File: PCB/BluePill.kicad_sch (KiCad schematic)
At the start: 36 parts, among them J1 USB_B_Micro, J2 Conn_01x20, J3 Conn_02x03_Odd_Even, J4 Conn_01x20, J5 Conn_01x04, SW1 SW_Push, U1 STM32F103C8Tx, U2 RT9193-33, Y1 Crystal_GND24_Small, Y2 8MHZ

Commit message: 更换USB插座封装
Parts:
- J1: value USB_B_Micro -> (none); footprint Connector_USB:USB_Micro-B_Molex_47346-0001 -> (none)
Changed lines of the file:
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@@
     (in_bom yes) (on_board yes) (fields_autoplaced)
     (property "Reference" "J1" (id 0) (at 43.18 19.05 0))
-    (property "Value" "USB_B_Micro" (id 1) (at 43.18 21.59 0))
-    (property "Footprint" "Connector_USB:USB_Micro-B_Molex_47346-0001" (id 2) (at 46.99 33.02 0)
+    (property "Value" "" (id 1) (at 43.18 21.59 0))
+    (property "Footprint" "" (id 2) (at 46.99 33.02 0)
       (effects (font (size 1.27 1.27)) hide)
     )
@@
     )
     (path "/5e707534-c918-46f7-a5cb-689e5a18b5bb"
-      (reference "J1") (unit 1) (value "USB_B_Micro") (footprint "Connector_USB:USB_Micro-B_Molex_47346-0001")
+      (reference "J1") (unit 1) (value "USB_B_Micro") (footprint "Connector_USB:USB_Micro-B_Molex-105017-0001")
     )
     (path "/7870a9db-0a4b-4ce4-a426-dcf645359822"

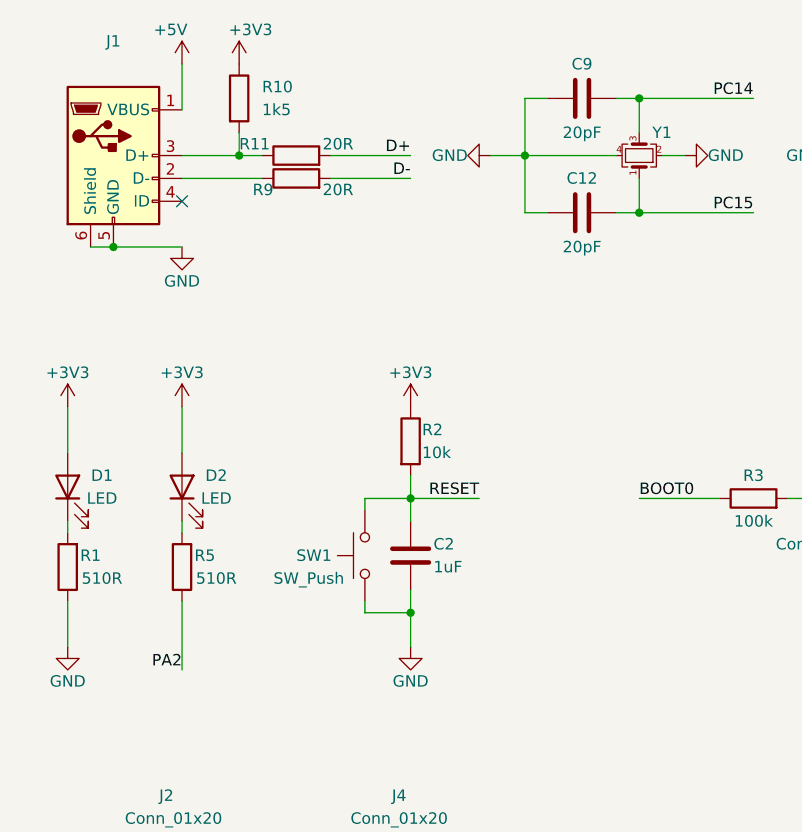
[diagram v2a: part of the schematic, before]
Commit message: 修复32K晶振问题；局部优化。
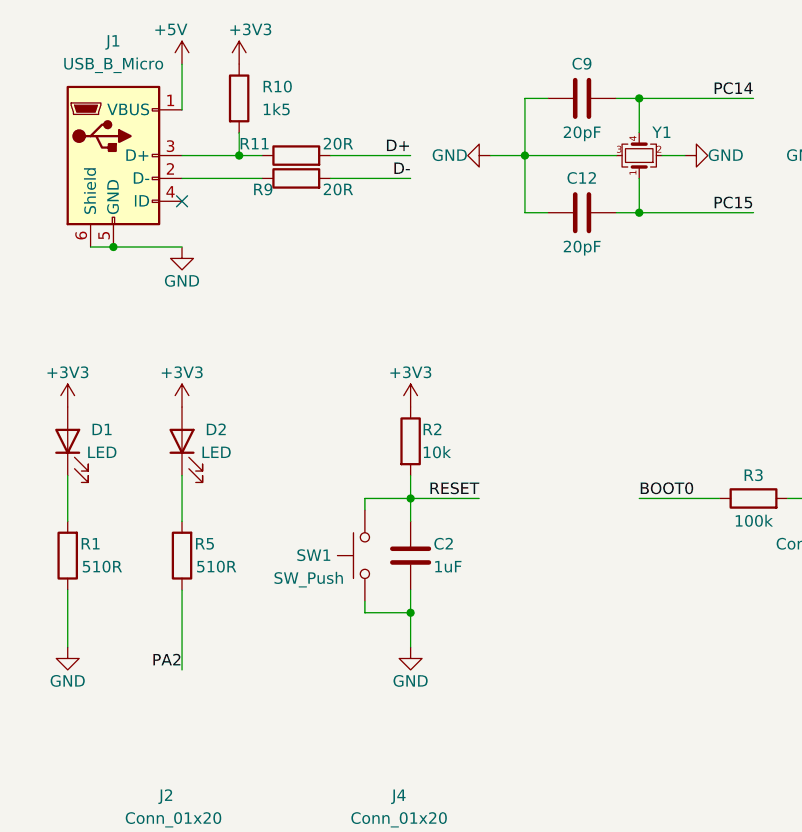
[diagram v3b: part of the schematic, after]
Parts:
- J1: value (none) -> USB_B_Micro; footprint (none) -> Connector_USB:USB_Micro-B_Molex-105017-0001
- Y1: value Crystal_GND24_Small -> (none); footprint Crystal:Crystal_SMD_SeikoEpson_MC306-4Pin_8.0x3.2mm -> (none); symbol Device:Crystal_GND24_Small -> Device:Crystal_GND23_Small
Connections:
- net GND: now also Y1.3; no longer Y1.4
- net PC14: now also Y1.4; no longer Y1.3
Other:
- moved on the sheet: D1, D2, R1, R5
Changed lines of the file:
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@@
+    (stroke (width 0) (type default) (color 0 0 0 0))
+  )
+  (wire (pts (xy 50.8 67.31) (xy 50.8 72.39))
     (stroke (width 0) (type default) (color 0 0 0 0))
   )
@@
     (stroke (width 0) (type default) (color 0 0 0 0))
   )
-  (wire (pts (xy 38.1 73.66) (xy 38.1 72.39))
-    (stroke (width 0) (type default) (color 0 0 0 0))
-  )
   (wire (pts (xy 106.68 31.75) (xy 104.14 31.75))
     (stroke (width 0) (type default) (color 0 0 0 0))
@@
     (stroke (width 0) (type default) (color 0 0 0 0))
   )
-  (wire (pts (xy 50.8 81.28) (xy 50.8 88.9))
+  (wire (pts (xy 50.8 80.01) (xy 50.8 88.9))
     (stroke (width 0) (type default) (color 0 0 0 0))
   )
@@
     (stroke (width 0) (type default) (color 0 0 0 0))
   )
-  (wire (pts (xy 38.1 59.69) (xy 38.1 64.77))
-    (stroke (width 0) (type default) (color 0 0 0 0))
-  )
   (wire (pts (xy 38.1 139.7) (xy 44.45 139.7))
     (stroke (width 0) (type default) (color 0 0 0 0))
@@
     (stroke (width 0) (type default) (color 0 0 0 0))
   )
-  (wire (pts (xy 50.8 59.69) (xy 50.8 64.77))
-    (stroke (width 0) (type default) (color 0 0 0 0))
-  )
   (wire (pts (xy 101.6 176.53) (xy 110.49 176.53))
     (stroke (width 0) (type default) (color 0 0 0 0))
@@
     (stroke (width 0) (type default) (color 0 0 0 0))
   )
+  (wire (pts (xy 38.1 67.31) (xy 38.1 72.39))
+    (stroke (width 0) (type default) (color 0 0 0 0))
+  )
   (wire (pts (xy 130.81 104.14) (xy 130.81 105.41))
     (stroke (width 0) (type default) (color 0 0 0 0))
@@
     (stroke (width 0) (type default) (color 0 0 0 0))
   )
-  (wire (pts (xy 38.1 81.28) (xy 38.1 86.36))
+  (wire (pts (xy 38.1 80.01) (xy 38.1 86.36))
     (stroke (width 0) (type default) (color 0 0 0 0))
   )
@@
     (stroke (width 0) (type default) (color 0 0 0 0))
   )
-  (wire (pts (xy 50.8 72.39) (xy 50.8 73.66))
-    (stroke (width 0) (type default) (color 0 0 0 0))
-  )
   (wire (pts (xy 215.9 73.66) (xy 215.9 80.01))
     (stroke (width 0) (type default) (color 0 0 0 0))
@@
     (effects (font (size 1.27 1.27)) (justify right bottom))
   )
-  (symbol (lib_id "Device:R") (at 38.1 77.47 180) (unit 1)
-    (in_bom yes) (on_board yes)
-    (property "Reference" "R1" (id 0) (at 40.64 76.2 0))
-    (property "Value" "510R" (id 1) (at 41.91 78.74 0))
-    (property "Footprint" "Capacitor_SMD:C_0603_1608Metric" (id 2) (at 39.878 77.47 90)
-      (effects (font (size 1.27 1.27)) hide)
-    )
-    (property "Datasheet" "~" (id 3) (at 38.1 77.47 0)
+  (symbol (lib_id "Device:R") (at 38.1 76.2 180) (unit 1)
+    (in_bom yes) (on_board yes)
+    (property "Reference" "R1" (id 0) (at 40.64 74.93 0))
+    (property "Value" "510R" (id 1) (at 41.91 77.47 0))
+    (property "Footprint" "Capacitor_SMD:C_0603_1608Metric" (id 2) (at 39.878 76.2 90)
+      (effects (font (size 1.27 1.27)) hide)
+    )
+    (property "Datasheet" "~" (id 3) (at 38.1 76.2 0)
       (effects (font (size 1.27 1.27)) hide)
     )
@@
     (in_bom yes) (on_board yes) (fields_autoplaced)
     (property "Reference" "J1" (id 0) (at 43.18 19.05 0))
-    (property "Value" "" (id 1) (at 43.18 21.59 0))
-    (property "Footprint" "" (id 2) (at 46.99 33.02 0)
+    (property "Value" "USB_B_Micro" (id 1) (at 43.18 21.59 0))
+    (property "Footprint" "Connector_USB:USB_Micro-B_Molex-105017-0001" (id 2) (at 46.99 33.02 0)
       (effects (font (size 1.27 1.27)) hide)
     )
@@
     (pin "6")
   )
-  (symbol (lib_id "Device:LED") (at 50.8 68.58 90) (unit 1)
-    (in_bom yes) (on_board yes)
-    (property "Reference" "D2" (id 0) (at 54.61 67.31 90))
-    (property "Value" "LED" (id 1) (at 54.61 69.85 90))
-    (property "Footprint" "Capacitor_SMD:C_0603_1608Metric" (id 2) (at 50.8 68.58 0)
-      (effects (font (size 1.27 1.27)) hide)
-    )
-    (property "Datasheet" "~" (id 3) (at 50.8 68.58 0)
+  (symbol (lib_id "Device:LED") (at 50.8 63.5 90) (unit 1)
+    (in_bom yes) (on_board yes)
+    (property "Reference" "D2" (id 0) (at 54.61 62.23 90))
+    (property "Value" "LED" (id 1) (at 54.61 64.77 90))
+    (property "Footprint" "Capacitor_SMD:C_0603_1608Metric" (id 2) (at 50.8 63.5 0)
+      (effects (font (size 1.27 1.27)) hide)
+    )
+    (property "Datasheet" "~" (id 3) (at 50.8 63.5 0)
       (effects (font (size 1.27 1.27)) hide)
     )
@@
     (pin "1")
   )
-  (symbol (lib_id "Device:R") (at 50.8 77.47 180) (unit 1)
-    (in_bom yes) (on_board yes)
-    (property "Reference" "R5" (id 0) (at 53.34 76.2 0))
-    (property "Value" "510R" (id 1) (at 54.61 78.74 0))
-    (property "Footprint" "Capacitor_SMD:C_0603_1608Metric" (id 2) (at 52.578 77.47 90)
-      (effects (font (size 1.27 1.27)) hide)
-    )
-    (property "Datasheet" "~" (id 3) (at 50.8 77.47 0)
+  (symbol (lib_id "Device:R") (at 50.8 76.2 180) (unit 1)
+    (in_bom yes) (on_board yes)
+    (property "Reference" "R5" (id 0) (at 53.34 74.93 0))
+    (property "Value" "510R" (id 1) (at 54.61 77.47 0))
+    (property "Footprint" "Capacitor_SMD:C_0603_1608Metric" (id 2) (at 52.578 76.2 90)
+      (effects (font (size 1.27 1.27)) hide)
+    )
+    (property "Datasheet" "~" (id 3) (at 50.8 76.2 0)
       (effects (font (size 1.27 1.27)) hide)
     )
@@
     (pin "1")
   )
-  (symbol (lib_id "Device:Crystal_GND24_Small") (at 101.6 31.75 90) (unit 1)
+  (symbol (lib_id "Device:Crystal_GND23_Small") (at 101.6 31.75 90) (unit 1)
     (in_bom yes) (on_board yes)
     (property "Reference" "Y1" (id 0) (at 104.14 29.21 90))
-    (property "Value" "Crystal_GND24_Small" (id 1) (at 104.14 27.94 90)
-      (effects (font (size 1.27 1.27)) hide)
-    )
-    (property "Footprint" "Crystal:Crystal_SMD_SeikoEpson_MC306-4Pin_8.0x3.2mm" (id 2) (at 101.6 31.75 0)
+    (property "Value" "" (id 1) (at 104.14 27.94 90)
+      (effects (font (size 1.27 1.27)) hide)
+    )
+    (property "Footprint" "" (id 2) (at 101.6 31.75 0)
       (effects (font (size 1.27 1.27)) hide)
     )
@@
     (pin "1")
   )
-  (symbol (lib_id "Device:LED") (at 38.1 68.58 90) (unit 1)
-    (in_bom yes) (on_board yes)
-    (property "Reference" "D1" (id 0) (at 41.91 67.31 90))
-    (property "Value" "LED" (id 1) (at 41.91 69.85 90))
-    (property "Footprint" "Capacitor_SMD:C_0603_1608Metric" (id 2) (at 38.1 68.58 0)
-      (effects (font (size 1.27 1.27)) hide)
-    )
-    (property "Datasheet" "~" (id 3) (at 38.1 68.58 0)
-      (effects (font (size 1.27 1.27)) hide)
-    )
+  (symbol (lib_id "Device:LED") (at 38.1 63.5 90) (unit 1)
+    (in_bom yes) (on_board yes)
+    (property "Reference" "D1" (id 0) (at 41.91 62.23 90))
+    (property "Value" "LED" (id 1) (at 41.91 64.77 90))
+    (property "Footprint" "Capacitor_SMD:C_0603_1608Metric" (id 2) (at 38.1 63.5 0)
+      (effects (font (size 1.27 1.27)) hide)
+    )
+    (property "Datasheet" "~" (id 3) (at 38.1 63.5 0)
+      (effects (font (size 1.27 1.27)) hide)
+    )
